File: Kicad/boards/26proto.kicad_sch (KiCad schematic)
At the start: 50 parts, among them J1 5051104096, J10 Conn_01x05, J2 Micro_SD_Card, J3 URM37, J4 RE12A, J5 RS485_TFT, J6 RS485_airdata, J7 RS485_logger_2, J8 RS485_logger, J9 BNO085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

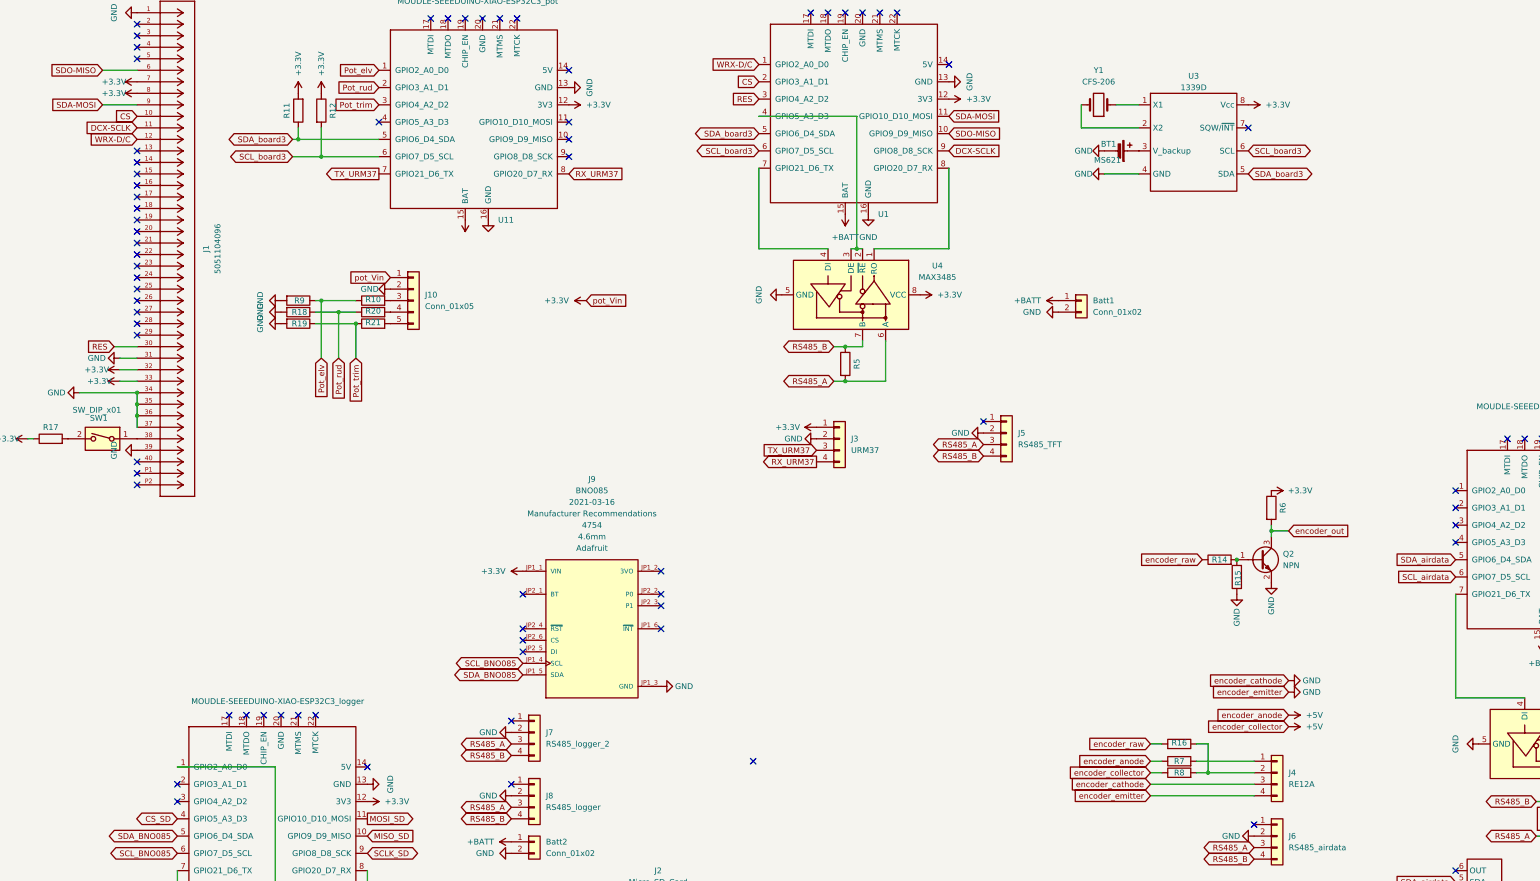
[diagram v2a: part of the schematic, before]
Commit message: added LED
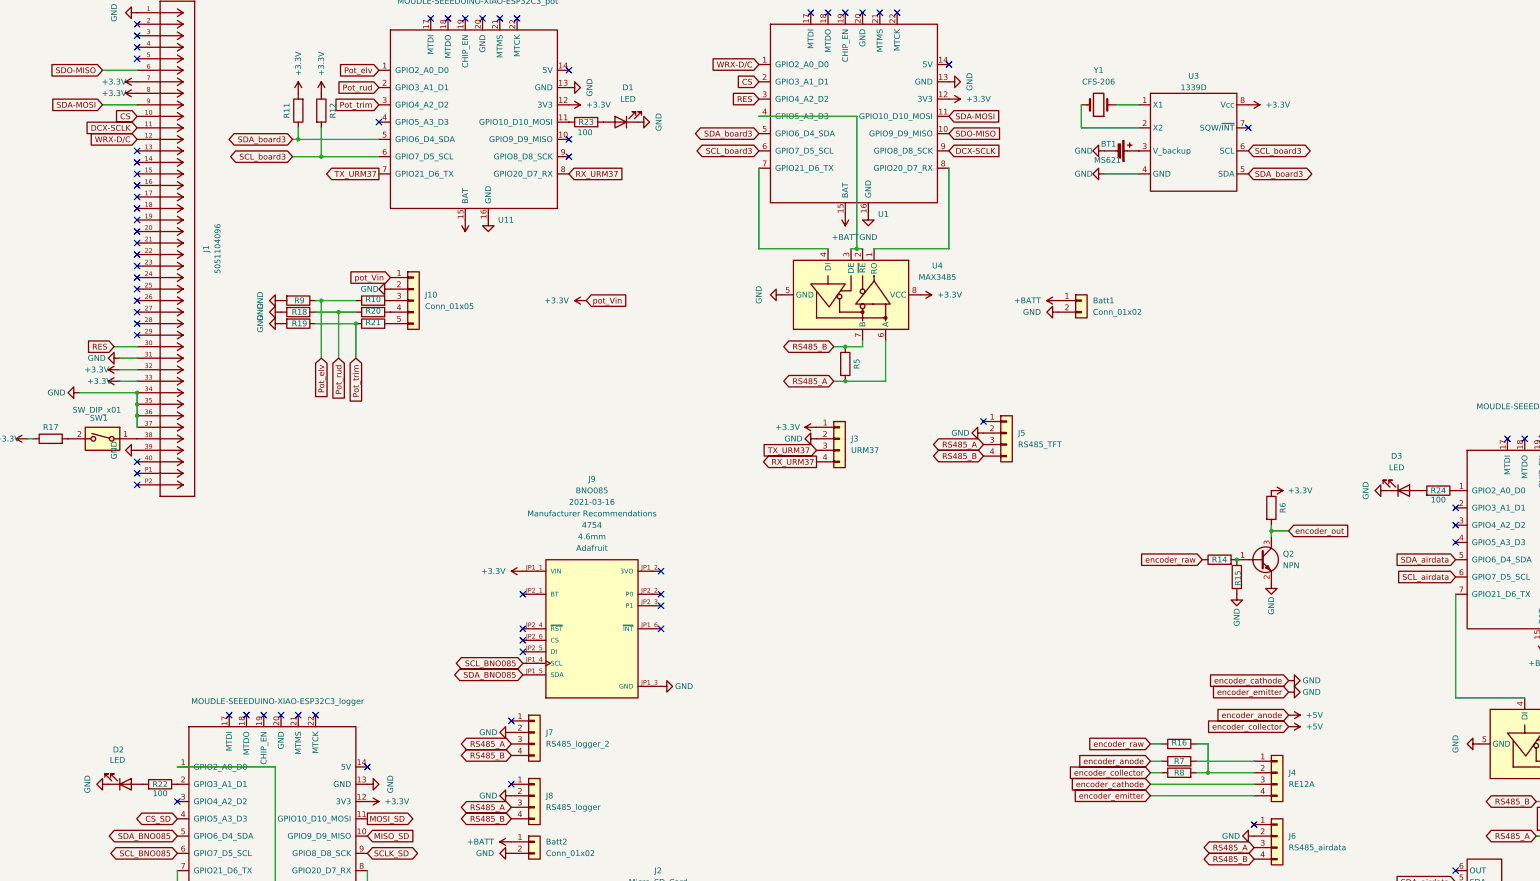
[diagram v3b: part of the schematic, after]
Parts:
- added D1, D2, D3: LED, LED_SMD:LED_0603_1608Metric_Pad1.05x0.95mm_HandSolder, symbol Device:LED
- added R22, R23, R24: 100, Resistor_SMD:R_0603_1608Metric_Pad0.98x0.95mm_HandSolder, symbol Device:R
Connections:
- net GND: now also D1.1 (K), D2.1 (K), D3.1 (K)
- net at U11.11 (GPIO10_D10_MOSI): now also R23.1
- net at U5.2 (GPIO3_A1_D1): now also R22.1
- net at U7.1 (GPIO2_A0_D0): now also R24.1
- new net: D2.2 (A), R22.2
- new net: D3.2 (A), R24.2
- new net: D1.2 (A), R23.2
- no-connect marks 83 -> 79

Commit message: added jumper
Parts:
- added JP1: SolderJumper_2_Open, Jumper:SolderJumper-2_P1.3mm_Open_TrianglePad1.0x1.5mm, symbol Jumper:SolderJumper_2_Open
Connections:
- net at J1.38, SW1.1: now also JP1.2 (B)
- net at R17.2, SW1.2: now also JP1.1 (A)
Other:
- note added: "1. airdata"
- note added: "2. logger and IMU"
- note added: "3. TFT, potentiometer, RTC and ultrasonic sensor"
- moved on the sheet: AS5600, AS5601, BT1, Batt1, Batt2, Batt3, C1, D1, D2, D3, DPS310, J1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
